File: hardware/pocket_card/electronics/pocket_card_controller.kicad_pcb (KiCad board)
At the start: 2 copper layers, 80.5 x 37 mm, 17 parts, among them U1 SOIC-28W_7.5x17.9mm_P1.27mm

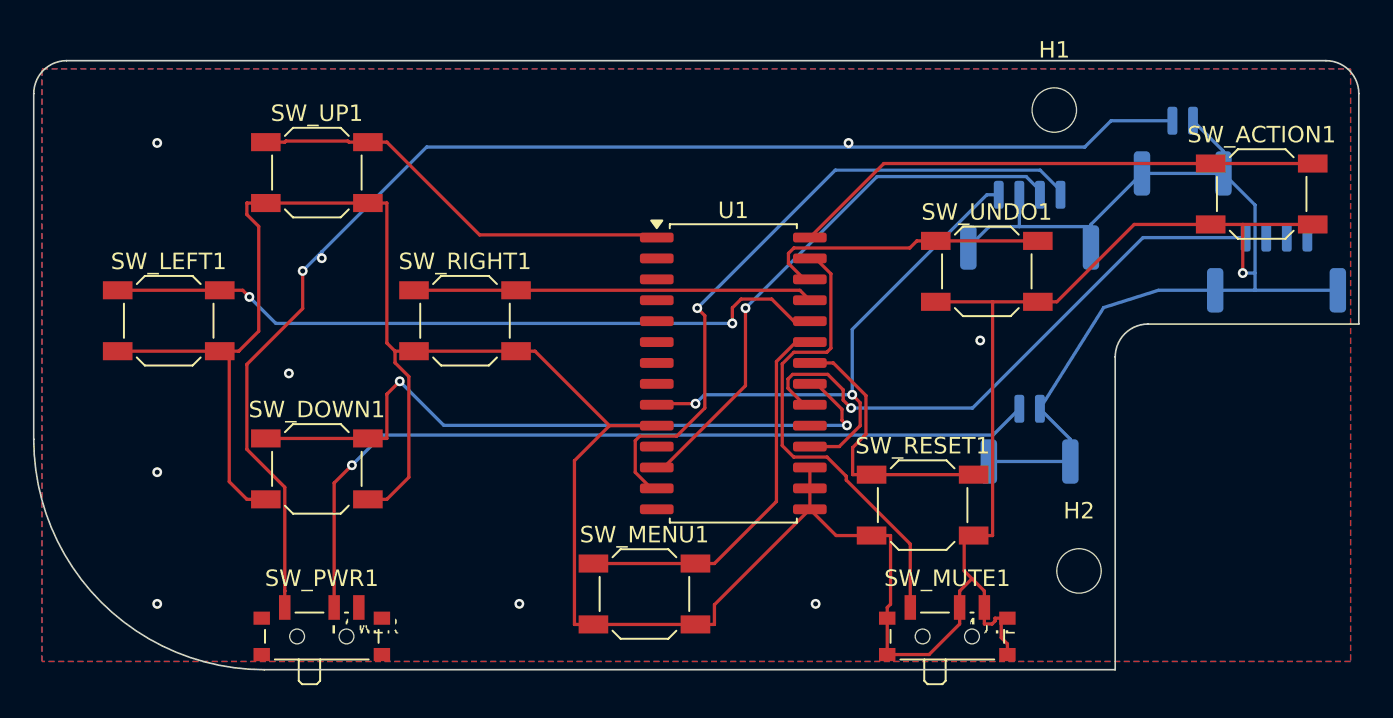
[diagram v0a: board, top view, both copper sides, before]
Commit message: feat: relocate Pocket Card Reset and lower mount
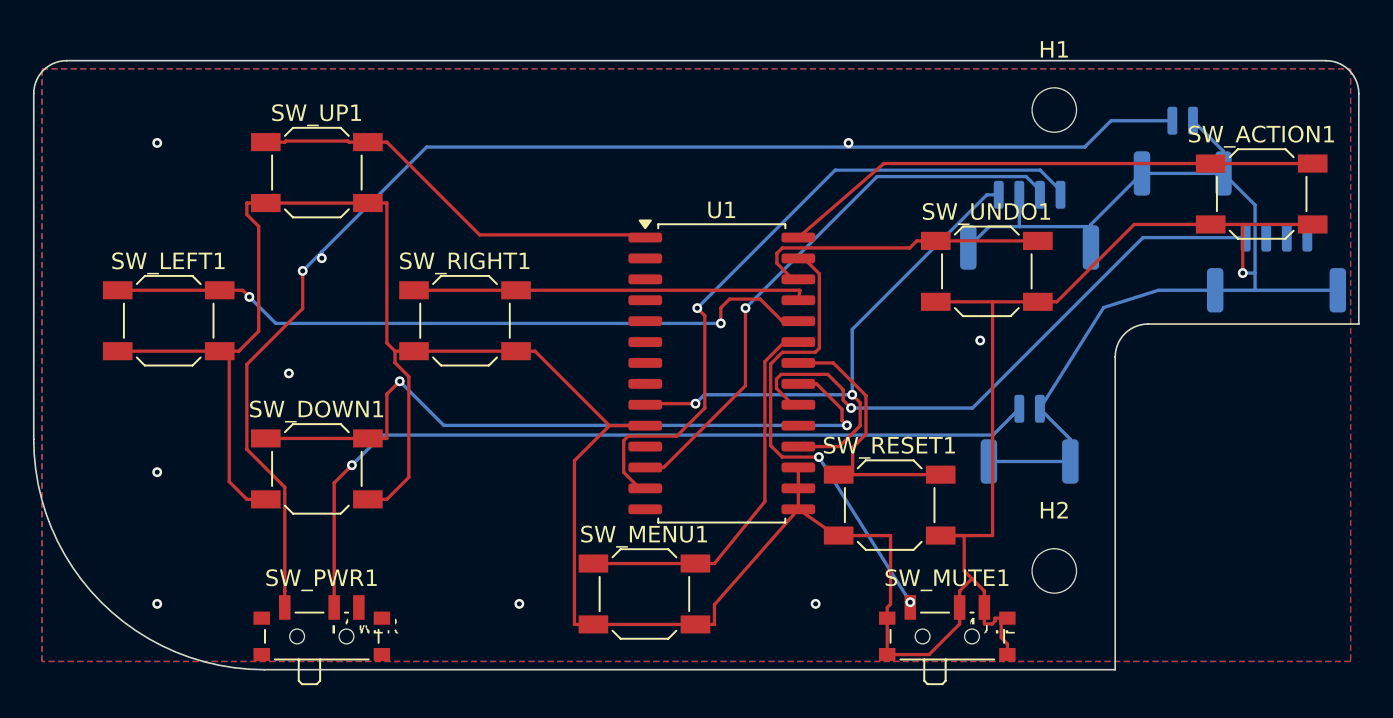
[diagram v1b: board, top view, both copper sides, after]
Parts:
- moved SW_RESET1 2.00 mm to (54.5, 80.0)
- moved H2 1.50 mm to (64.5, 84.0)
- moved U1 0.70 mm to (44.3, 72.0)
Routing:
- net GND: track 246.2 -> 248.4 mm
- net +3V3: track 34.0 -> 35.4 mm
- net SIG_UNDO: track 17.8 -> 18.5 mm
- net SDA: track 41.3 -> 42.0 mm
- net SCL: track 34.0 -> 34.7 mm
- net SIG_LEFT: track 44.6 -> 43.9 mm
- net SIG_DOWN: track 43.1 -> 43.8 mm
- net INT: track 35.7 -> 36.4 mm
- net SIG_ACTION: track 32.4 -> 32.9 mm
- net SIG_MUTE: track 28.7 -> 28.5 mm, vias 0 -> 2
